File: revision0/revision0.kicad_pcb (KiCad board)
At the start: 2 copper layers, 50 x 50 mm, 36 parts, among them J1 USB1, J10 Conn_01x03, J2 Conn_01x07, J3 Conn_02x03_Counter_Clockwise, J4 Conn_01x05, J5 Conn_02x03_Counter_Clockwise, J6 Conn_02x03_Counter_Clockwise, J7 Conn_02x03_Counter_Clockwise, J8 Conn_01x04, J9 Conn_01x03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

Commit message: minor fix
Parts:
- removed D8: CLX6F-FKC, LED_SMD:LED_RGB_PLCC-6
- removed J10: Conn_01x03, Connector_PinHeader_2.54mm:PinHeader_1x03_P2.54mm_Vertical
- removed R9: 1k, Resistor_SMD:R_0805_2012Metric_Pad1.20x1.40mm_HandSolder
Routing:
- net Net-(D8-KB): track 8.66 -> 0.00 mm
- net Net-(D8-AB): track 7.75 -> 0.00 mm
- net Net-(D8-AG): track 5.99 -> 0.00 mm
- net Net-(D8-AR): track 4.70 -> 0.00 mm
- net GND: track 37.5 -> 33.3 mm, vias 4 -> 3
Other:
- board text added: "D3-D6"
- board text removed: "R G B"

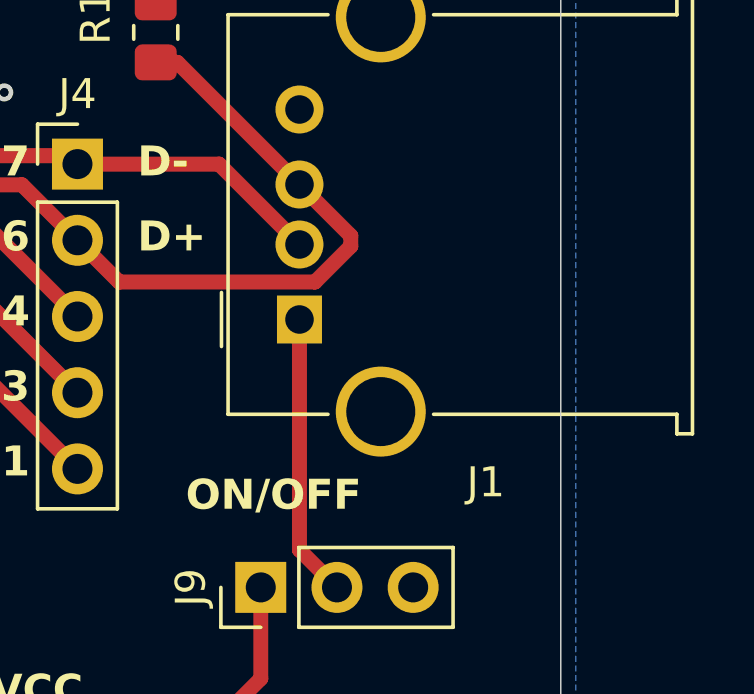
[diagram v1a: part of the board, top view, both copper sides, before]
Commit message: update project w/ missing footprint
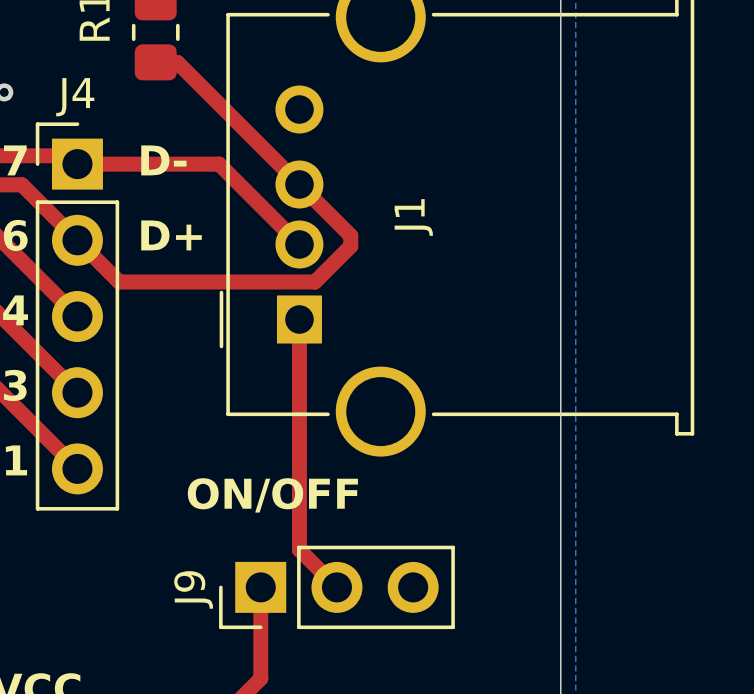
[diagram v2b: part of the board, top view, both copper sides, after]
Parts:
- J1: footprint Library:USB_A_Molex_67643_Horizontal -> usb:USB_A_Molex_67643_Horizontal
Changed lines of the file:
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@@
 		)
 	)
-	(footprint "Library:USB_A_Molex_67643_Horizontal"
+	(footprint "usb:USB_A_Molex_67643_Horizontal"
 		(layer "F.Cu")
 		(at 141.29 80.07 90)
@@
 		(tags "USB_A Female Connector receptacle")
 		(property "Reference" "J1"
-			(at -5.43 6.21 180)
+			(at 3.5 3.71 90)
 			(layer "F.SilkS")
 			(effects
@@
 			)
 		)
-		(property "Footprint" "Library:USB_A_Molex_67643_Horizontal"
+		(property "Footprint" "usb:USB_A_Molex_67643_Horizontal"
 			(at 0 0 90)
 			(layer "F.Fab")
@@
 		)
 		(fp_text user "${REFERENCE}"
-			(at 4.07 5.21 90)
-			(layer "F.Fab")
-			(effects
+			(at 3.5 3.7 90)
+			(layer "F.Fab")
+			(effects
